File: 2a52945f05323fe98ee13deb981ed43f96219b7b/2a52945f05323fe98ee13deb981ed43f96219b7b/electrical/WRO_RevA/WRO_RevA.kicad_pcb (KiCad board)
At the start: 2 copper layers, 75 x 58 mm, 31 parts, among them J1 VCC, J2 MPU6050, J3 TO_PI, J4 SERVO, J5 MOTOR, SW1 EXEC_PRGM, U1 ESP32-DEVKIT-V1, U2 ROB-14450

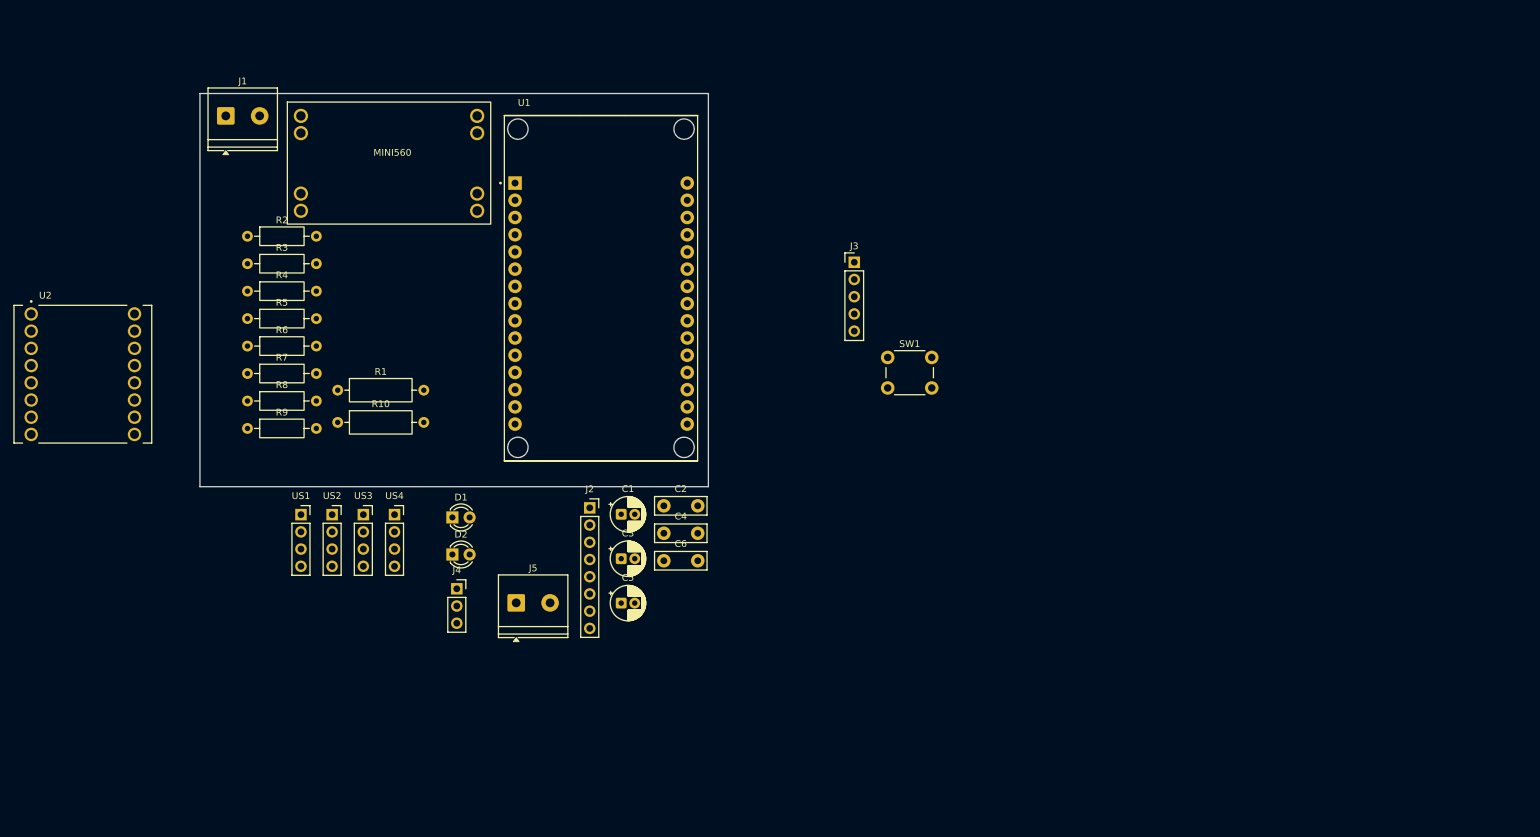
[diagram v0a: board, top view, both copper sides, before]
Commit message: minor changes to PCB
Lvl shifter still too big. have to mod ultrasonics....
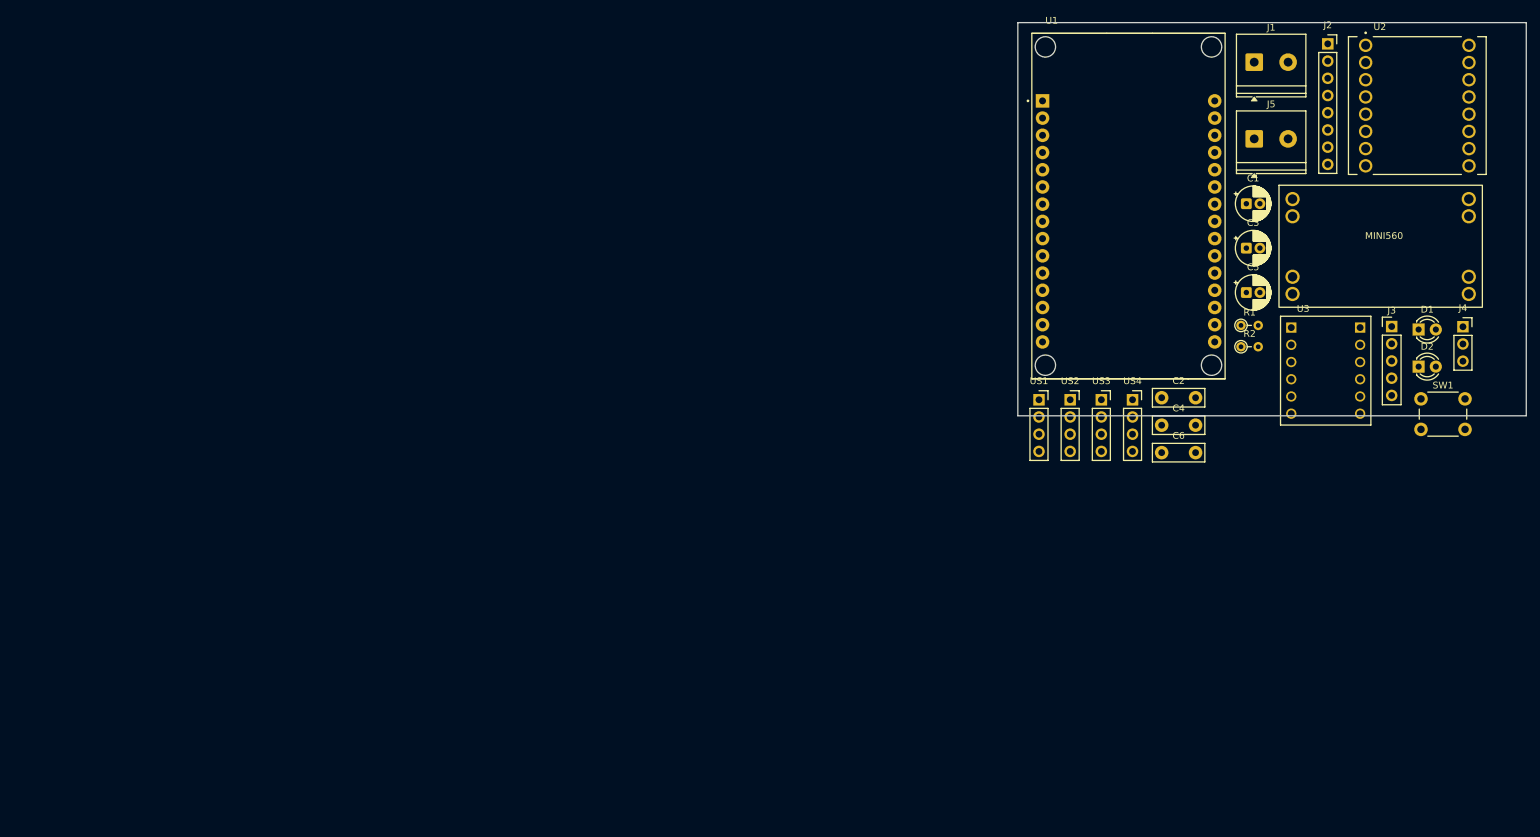
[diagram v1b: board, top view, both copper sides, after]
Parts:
- removed R10: 330, Resistor_THT:R_Axial_DIN0309_L9.0mm_D3.2mm_P12.70mm_Horizontal
- removed R3, R4, R6, R8: 4.7k, Resistor_THT:R_Axial_DIN0207_L6.3mm_D2.5mm_P10.16mm_Horizontal
- removed R5, R7, R9: 2.7k, Resistor_THT:R_Axial_DIN0207_L6.3mm_D2.5mm_P10.16mm_Horizontal
- added U3: BOB-12009, Snapeda:CONV_BOB-12009, F.Cu at (234.4, 79.5)
- R1: footprint Resistor_THT:R_Axial_DIN0309_L9.0mm_D3.2mm_P12.70mm_Horizontal -> Resistor_THT:R_Axial_DIN0204_L3.6mm_D1.6mm_P2.54mm_Vertical
- R2: value 2.7k -> 330; footprint Resistor_THT:R_Axial_DIN0207_L6.3mm_D2.5mm_P10.16mm_Horizontal -> Resistor_THT:R_Axial_DIN0204_L3.6mm_D1.6mm_P2.54mm_Vertical
- moved U2 200.8 mm to (247.9, 40.4)
- moved J4 153.4 mm to (254.6, 73.0)
- moved J1 151.9 mm to (223.8, 34.0)
- moved R2 147.5 mm to (221.9, 76.0)
- moved MINI560 146.8 mm to (242.5, 61.1)
- moved D1 145.2 mm to (248.1, 73.4)
- moved D2 145.2 mm to (248.1, 78.9)
- moved R1 133.6 mm to (221.9, 72.8)
- moved J2 128.6 mm to (234.7, 31.3)
- moved J5 128.6 mm to (223.8, 45.3)
- moved US3 110.2 mm to (201.3, 83.8)
- moved US4 110.2 mm to (205.9, 83.8)
- moved US1 110.2 mm to (192.1, 83.8)
- moved US2 110.2 mm to (196.7, 83.8)
- moved C1 103.0 mm to (222.7, 54.9)
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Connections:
- R2 pad 1: ECHO1 -> Net-(D2-K)
- R2 pad 2: Net-(US1-Pin_2) -> GND
- U1 pad 24: ECHO4 -> unconnected-(U1-D26-Pad24)
- U1 pad 25: TRIG4 -> unconnected-(U1-D27-Pad25)
- U1 pad 26: TRIG3 -> unconnected-(U1-D14-Pad26)
- U1 pad 27: TRIG2 -> unconnected-(U1-D12-Pad27)
- U1 pad 28: ECHO3 -> unconnected-(U1-D13-Pad28)
- U1 pad 4: ECHO1 -> unconnected-(U1-D2-Pad4)
- U1 pad 5: TRIG1 -> ECHO1_L
- U1 pad 8: ECHO2 -> TRIG1
- US1 pad 2: Net-(US1-Pin_2) -> ECHO1
- US2 pad 1: unconnected-(US2-Pin_1-Pad1) -> GND
- US2 pad 2: unconnected-(US2-Pin_2-Pad2) -> ECHO2
- US3 pad 2: Net-(US3-Pin_2) -> ECHO3
- US4 pad 2: Net-(US4-Pin_2) -> ECHO4

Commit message: minor changes
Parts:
- removed C1, C5: 1000uF, Capacitor_THT:CP_Radial_D5.0mm_P2.00mm
- removed C2, C4, C6: 0.1uF, Capacitor_THT:C_Disc_D7.5mm_W2.5mm_P5.00mm
- removed C3: 470uF, Capacitor_THT:CP_Radial_D5.0mm_P2.00mm
- removed D1: PWR, LED_THT:LED_D3.0mm
- removed D2: READY, LED_THT:LED_D3.0mm
- removed J1: VCC, TerminalBlock_Phoenix:TerminalBlock_Phoenix_PT-1,5-2-5.0-H_1x02_P5.00mm_Horizontal
- removed J2: MPU6050, Connector_PinSocket_2.54mm:PinSocket_1x08_P2.54mm_Vertical
- removed J3: TO_PI, Connector_PinHeader_2.54mm:PinHeader_1x05_P2.54mm_Vertical
- removed J4: SERVO, Connector_PinSocket_2.54mm:PinSocket_1x03_P2.54mm_Vertical
- removed J5: MOTOR, TerminalBlock_Phoenix:TerminalBlock_Phoenix_PT-1,5-2-5.0-H_1x02_P5.00mm_Horizontal
- removed MINI560: V1, Libreria_mia:Mini560
- removed R1, R2: 330, Resistor_THT:R_Axial_DIN0204_L3.6mm_D1.6mm_P2.54mm_Vertical
- removed SW1: EXEC_PRGM, Button_Switch_THT:SW_PUSH_6mm
- removed U1: ESP32-DEVKIT-V1, Snapeda:MODULE_ESP32_DEVKIT_V1
- removed U2: ROB-14450, Snapeda:MODULE_ROB-14450
- removed U3: BOB-12009, Snapeda:CONV_BOB-12009
- removed US1, US2, US3, US4: ULTRASONIC, Connector_PinSocket_2.54mm:PinSocket_1x04_P2.54mm_Vertical
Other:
- board size 75 x 58 mm -> 75 x 57 mm

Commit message: final shape for PCB, only need to route
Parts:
- added C1: 470uF, Capacitor_THT:CP_Radial_D5.0mm_P2.00mm, F.Cu at (122.3, 45.6)
- added C2: 0.1uF, Capacitor_THT:C_Disc_D7.5mm_W2.5mm_P5.00mm, F.Cu at (127.4, 48.4)
- added C3: 470uF, Capacitor_THT:CP_Radial_D5.0mm_P2.00mm, F.Cu at (153.2, 54.4)
- added C4: 0.1uF, Capacitor_THT:C_Disc_D7.5mm_W2.5mm_P5.00mm, F.Cu at (151.7, 60.8)
- added D1: PWR, LED_THT:LED_D3.0mm, F.Cu at (104.3, 76.7)
- added D2: READY, LED_THT:LED_D3.0mm, F.Cu at (104.3, 83.2)
- added G***: LOGO, LogoFoxR_2:LogoFoxR_2, F.Cu at (184.2, 71.5)
- added J1: VCC, TerminalBlock_Phoenix:TerminalBlock_Phoenix_PT-1,5-2-5.0-H_1x02_P5.00mm_Horizontal, F.Cu at (126.0, 36.0)
- added J3: TO_PI, Connector_PinHeader_2.54mm:PinHeader_1x05_P2.54mm_Vertical, F.Cu at (105.5, 88.7)
- added J4: SERVO, Connector_PinSocket_2.54mm:PinSocket_1x03_P2.54mm_Vertical, F.Cu at (165.0, 49.9)
- added J5: MOTOR, TerminalBlock_Phoenix:TerminalBlock_Phoenix_PT-1,5-2-5.0-H_1x02_P5.00mm_Horizontal, F.Cu at (173.4, 108.9)
- added MINI560: V1, Libreria_mia:Mini560, F.Cu at (145.1, 39.0)
- added R1: 330, Resistor_THT:R_Axial_DIN0204_L3.6mm_D1.6mm_P2.54mm_Vertical, F.Cu at (103.9, 71.5)
- added R2: 330, Resistor_THT:R_Axial_DIN0204_L3.6mm_D1.6mm_P2.54mm_Vertical, F.Cu at (107.0, 71.5)
- added SW1: EXEC_PRGM, Button_Switch_THT:SW_PUSH_6mm, F.Cu at (172.6, 93.5)
- added U1: ESP32-DEVKITC-32D, ESP32-DEVKITC-32D:ESP32-DEVKITC-32D, F.Cu at (138.3, 105.2)
- added U2: ROB-14450, Snapeda:MODULE_ROB-14450, F.Cu at (122.8, 78.2)
- added U3: BOB-12009, Snapeda:CONV_BOB-12009, F.Cu at (138.6, 57.8)
- added U4: MPU6050, usini_sensors:module_mpu6050, F.Cu at (165.8, 84.3)
- added US1: ULTRASONIC, Connector_PinHeader_2.54mm:PinHeader_1x04_P2.54mm_Vertical, F.Cu at (122.2, 54.0)
- added US2: ULTRASONIC, Connector_PinHeader_2.54mm:PinHeader_1x04_P2.54mm_Vertical, F.Cu at (168.2, 63.0)
- added US3: ULTRASONIC, Connector_PinHeader_2.54mm:PinHeader_1x04_P2.54mm_Vertical, F.Cu at (105.6, 108.2)
- added US4: ULTRASONIC, Connector_PinHeader_2.54mm:PinHeader_1x04_P2.54mm_Vertical, F.Cu at (185.4, 103.2)
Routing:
- net +11.2V: track 0.00 -> 27.9 mm
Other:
- board size 75 x 57 mm -> 87.2 x 93.9 mm

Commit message: started routing, added CREEA logo
gracias gustavo creea
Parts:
- added G***: LOGO, LogoCREEA:LogoCREEA, F.Cu at (176.8, 74.3)
- C3: value 470uF -> 100uF
- J3: footprint Connector_PinHeader_2.54mm:PinHeader_1x05_P2.54mm_Vertical -> Connector_PinHeader_2.54mm:PinHeader_1x06_P2.54mm_Vertical
- moved J3 82.6 mm to (185.0, 111.2), turned to 180 degrees
- moved SW1 69.1 mm to (103.6, 96.2)
- moved US4 19.1 mm to (185.3, 84.1)
- moved J4 6.57 mm to (165.0, 56.5), turned to 180 degrees
- moved R1 5.67 mm to (105.3, 77.0)
- moved D1 5.66 mm to (105.5, 82.2)
- moved D2 5.66 mm to (105.5, 88.7)
- moved R2 5.59 mm to (108.0, 77.0)
- moved G*** 3.03 mm to (184.8, 74.5)
- moved U1 2.28 mm to (140.4, 106.0)
- moved US3 1.25 mm to (106.8, 108.2)
- moved J5 0.62 mm to (173.9, 109.2)
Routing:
- net Net-(D1-K): track 0.00 -> 5.27 mm
- net +11.2V: track 27.9 -> 24.7 mm
- net +5V: track 0.00 -> 2.54 mm

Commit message: finished
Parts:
- removed D1: PWR, LED_THT:LED_D3.0mm
- removed D2: READY, LED_THT:LED_D3.0mm
- removed J3: TO_PI, Connector_PinHeader_2.54mm:PinHeader_1x06_P2.54mm_Vertical
- added PWR: PWR, LED_THT:LED_D3.0mm, F.Cu at (109.1, 124.0)
- added READY: READY, LED_THT:LED_D3.0mm, F.Cu at (103.8, 124.0)
- added REF**: KiCad-Logo2_5mm_SilkScreen, Symbol:KiCad-Logo2_5mm_SilkScreen, F.Cu at (176.5, 106.6)
- added SW2: PWR, EasyEDA:SW-TH_L22.2-W15.0-P7.00_KCD1-2P-P, F.Cu at (139.1, 60.2)
- added TO_PI: TO_PI, Connector_PinHeader_2.54mm:PinHeader_1x06_P2.54mm_Vertical, F.Cu at (187.2, 135.4)
- J4: footprint Connector_PinSocket_2.54mm:PinSocket_1x03_P2.54mm_Vertical -> Connector_PinHeader_2.54mm:PinHeader_1x03_P2.54mm_Vertical
- R1, R2: footprint Resistor_THT:R_Axial_DIN0204_L3.6mm_D1.6mm_P2.54mm_Vertical -> Resistor_THT:R_Axial_DIN0204_L3.6mm_D1.6mm_P5.08mm_Horizontal
- moved US4 83.1 mm to (105.8, 108.2), turned to 180 degrees
- moved US3 79.9 mm to (186.8, 108.2), turned to 180 degrees
- moved U4 52.3 mm to (120.9, 111.2), turned to 0 degrees
- moved U2 42.9 mm to (156.4, 104.8), turned to -90 degrees
- moved R1 42.4 mm to (109.3, 119.2)
- moved R2 42.2 mm to (106.2, 119.2)
- moved SW1 41.0 mm to (111.0, 136.5), turned to 180 degrees
- moved US1 39.8 mm to (112.8, 92.6), turned to 135 degrees
- moved MINI560 39.4 mm to (155.0, 77.2)
- moved C3 34.4 mm to (154.3, 88.8), turned to -90 degrees
- moved US2 31.5 mm to (176.3, 93.4), turned to -135 degrees
- moved C4 28.5 mm to (160.6, 87.8), turned to -90 degrees
- moved G*** 27.8 mm to (173.1, 99.7)
- moved U3 25.4 mm to (128.9, 81.3), turned to 0 degrees
- moved G*** 25.4 mm to (179.8, 99.5)
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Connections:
- J1 pad 1: +11.2V -> GND
- J1 pad 2: GND -> Net-(J1-Pin_2)
- U1 pad J2-13: STBY -> unconnected-(U1-IO12-PadJ2-13)
- U2 pad 13: STBY -> +5V
- US2 pad 3: unconnected-(US2-Pin_3-Pad3) -> TRIG2
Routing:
- net +5V: track 2.54 -> 253.4 mm
- net +3V3: track 0.00 -> 127.3 mm, vias 0 -> 1
- net PRGM: track 0.00 -> 89.2 mm
- net SERVO: track 0.00 -> 83.2 mm, vias 0 -> 6
- net READY: track 0.00 -> 82.4 mm
- net SCL: track 0.00 -> 73.9 mm, vias 0 -> 4
- net TRIG2: track 0.00 -> 70.5 mm, vias 0 -> 3
- net ECHO3: track 0.00 -> 66.2 mm, vias 0 -> 2
- net ECHO2_L: track 0.00 -> 61.7 mm, vias 0 -> 5
- net RX: track 0.00 -> 61.1 mm
- net SDA: track 0.00 -> 59.6 mm, vias 0 -> 4
- net TX: track 0.00 -> 58.8 mm
- net TRIG3: track 0.00 -> 55.9 mm, vias 0 -> 6
- net ECHO2: track 0.00 -> 54.3 mm
- net ECHO3_L: track 0.00 -> 53.6 mm, vias 0 -> 2
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- added copper zone on B.Cu, net GND
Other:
- board text added: "+ -"
